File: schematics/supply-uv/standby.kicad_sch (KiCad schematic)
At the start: 106 parts, among them J5 CW2B-10A-T, K1 SRD-12VDC-SL-C, Q1 5N65F, Q2 IRLML5203, Q3 IRLML5203, Q4 IRLML5203, U10 TL331, U2 R7731, U3 EL817, U4 EL817, U5 L7805ABV, U6 L7805ABV, U7 TL431DBZ, U8 EL817, U9 TL432DBZ, Y1 B32022A3223M000

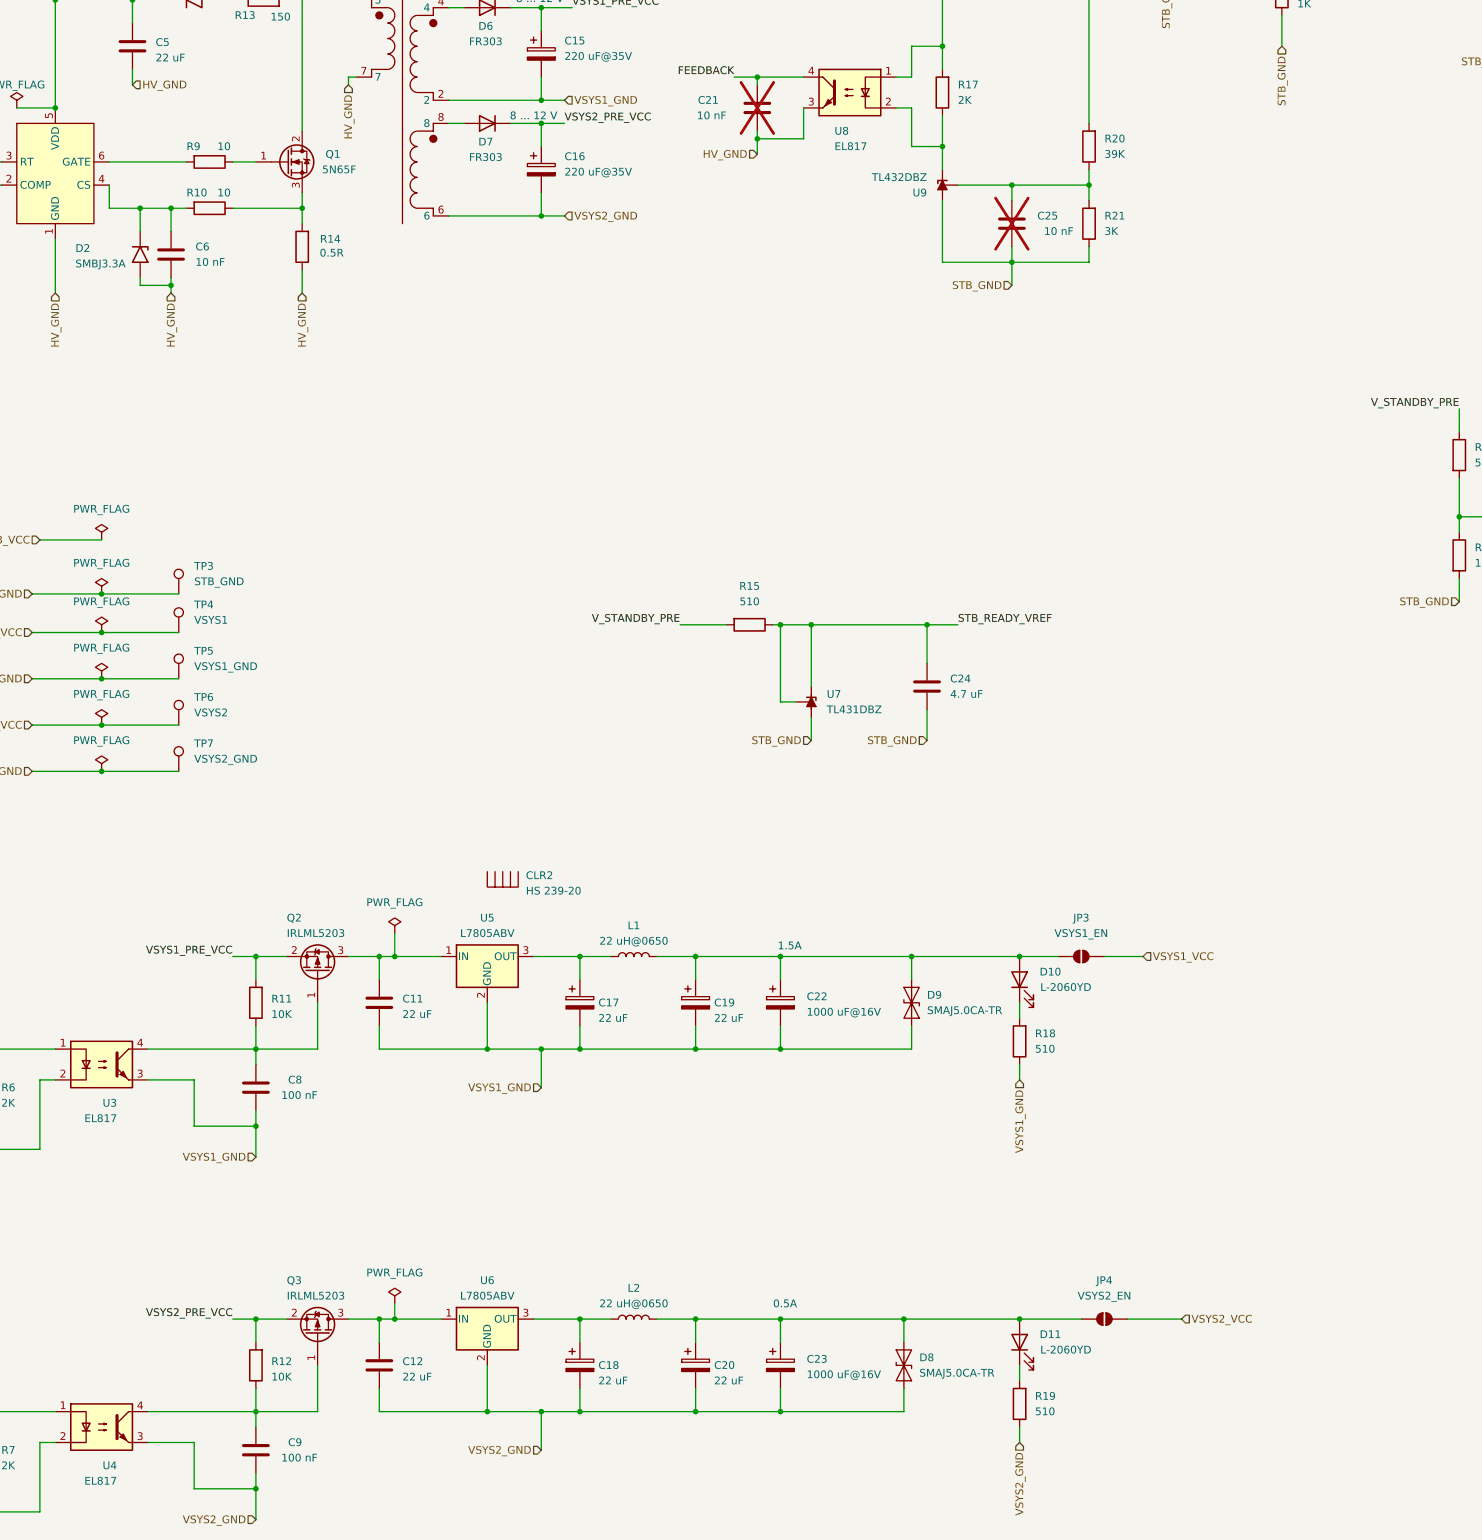
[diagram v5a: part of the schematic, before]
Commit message: some changes in board routing
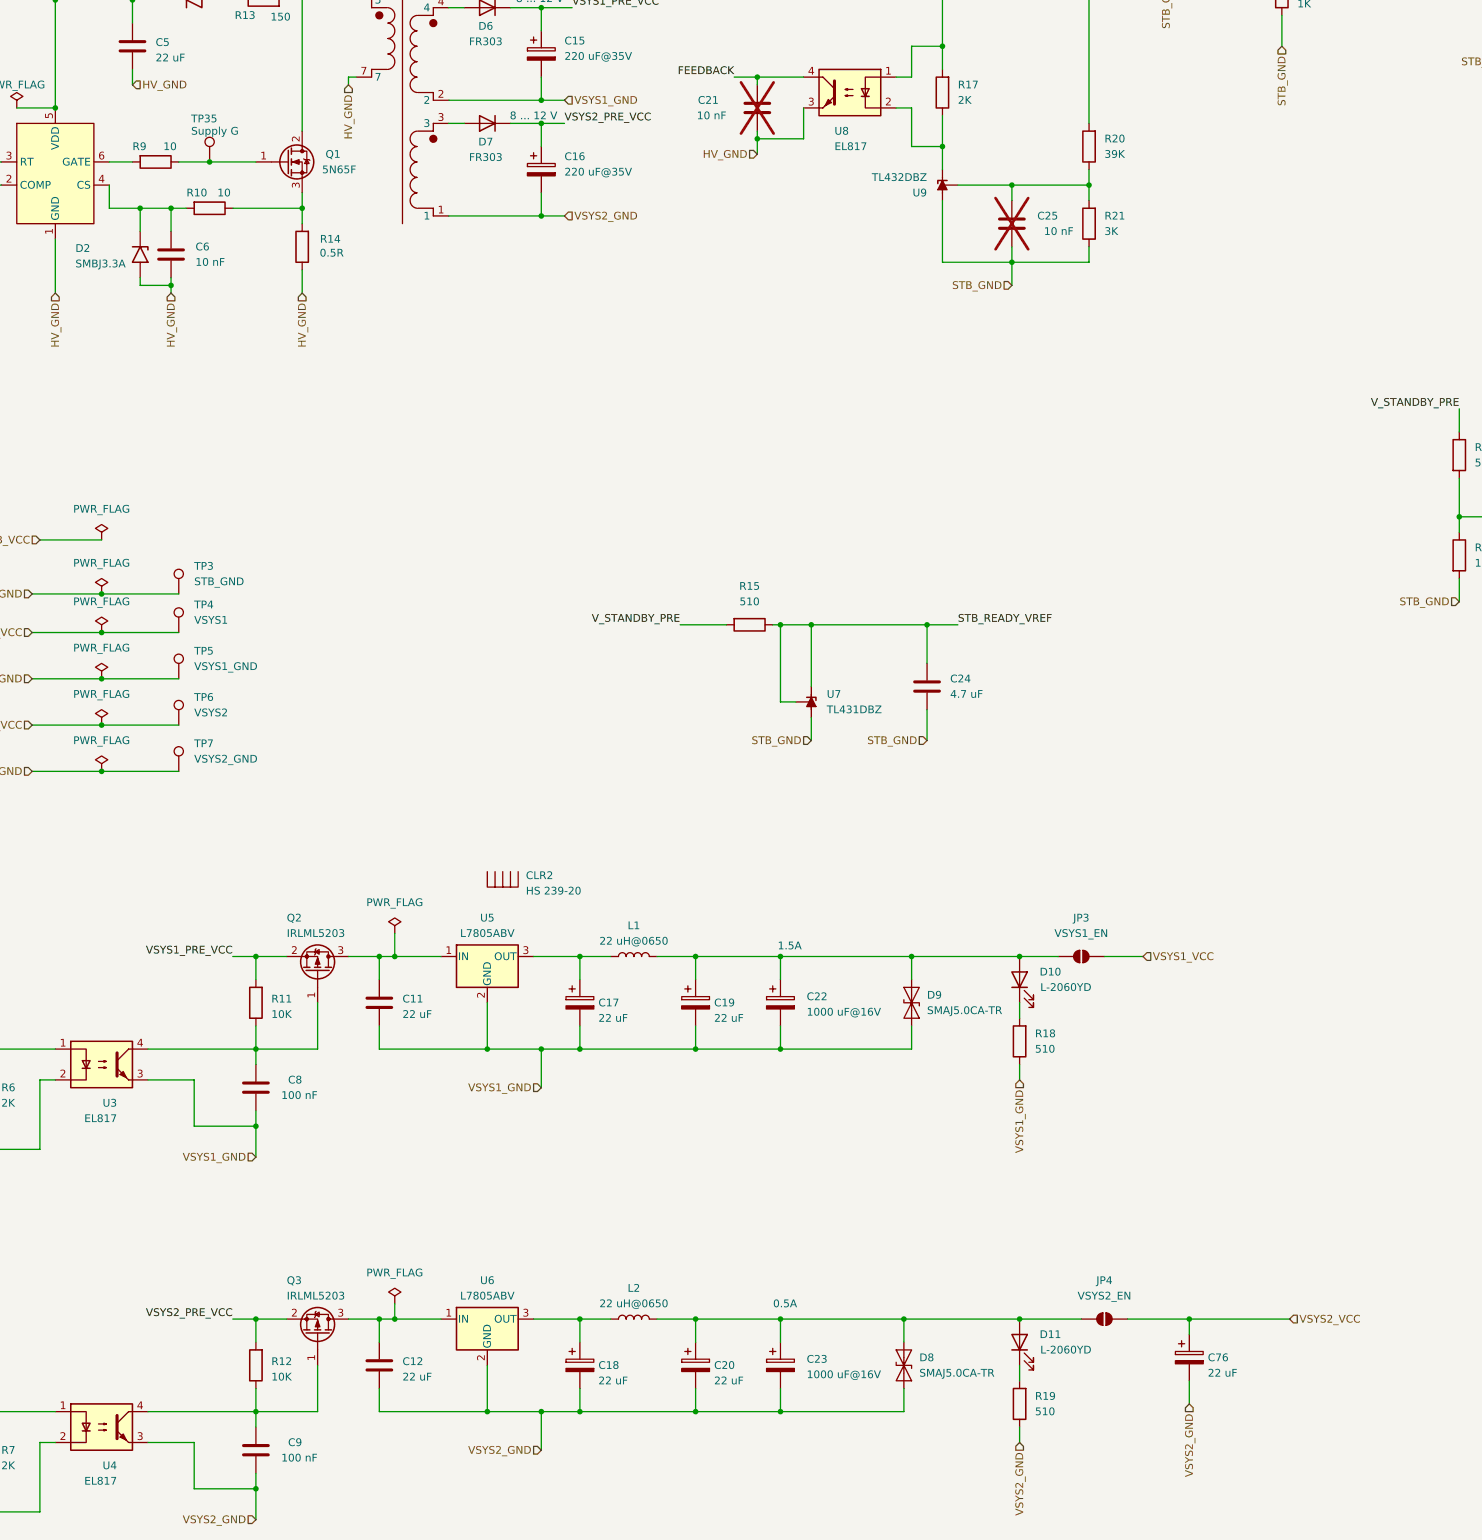
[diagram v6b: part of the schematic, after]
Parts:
- added C76: 22 uF, Capacitor_Tantalum_SMD:CP_EIA-3216-10_Kemet-I_Pad1.58x1.35mm_HandSolder, symbol Device:C_Polarized
- added TP35: Supply G, TestPoint:TestPoint_Pad_1.0x1.0mm, symbol Connector:TestPoint
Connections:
- net VSYS2_GND: now also TR1.1, C76.2; no longer TR1.6
- net VSYS2_VCC: now also C76.1
- net at D7.2 (A): now also TR1.3; no longer TR1.8
- net at Q1.1 (G), R9.1: now also TP35.1
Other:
- moved on the sheet: R9
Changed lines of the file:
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@@
 	)
 	(junction
+		(at 116.84 172.72)
+		(diameter 0)
+		(color 0 0 0 0)
+	)
+	(junction
 		(at 91.44 163.83)
 		(diameter 0)
@@
 	)
 	(junction
+		(at 278.13 363.22)
+		(diameter 0)
+		(color 0 0 0 0)
+	)
+	(junction
 		(at 124.46 331.47)
 		(diameter 0)
@@
 	(wire
 		(pts
+			(xy 116.84 172.72) (xy 124.46 172.72)
+		)
+		(stroke
+			(width 0)
+			(type default)
+		)
+	)
+	(wire
+		(pts
 			(xy 31.75 53.34) (xy 35.56 53.34)
 		)
@@
 	(wire
 		(pts
-			(xy 100.33 172.72) (xy 113.03 172.72)
+			(xy 100.33 172.72) (xy 104.14 172.72)
 		)
 		(stroke
@@
 	(wire
 		(pts
-			(xy 267.97 363.22) (xy 276.86 363.22)
+			(xy 267.97 363.22) (xy 278.13 363.22)
 		)
 		(stroke
@@
 	(wire
 		(pts
+			(xy 278.13 363.22) (xy 294.64 363.22)
+		)
+		(stroke
+			(width 0)
+			(type default)
+		)
+	)
+	(wire
+		(pts
 			(xy 332.74 128.27) (xy 332.74 132.08)
 		)
@@
 	(wire
 		(pts
+			(xy 278.13 363.22) (xy 278.13 365.76)
+		)
+		(stroke
+			(width 0)
+			(type default)
+		)
+	)
+	(wire
+		(pts
 			(xy 124.46 391.16) (xy 124.46 388.62)
 		)
@@
 	(wire
 		(pts
+			(xy 278.13 373.38) (xy 278.13 377.19)
+		)
+		(stroke
+			(width 0)
+			(type default)
+		)
+	)
+	(wire
+		(pts
 			(xy 104.14 41.91) (xy 104.14 43.18)
 		)
@@
 	(wire
 		(pts
-			(xy 120.65 172.72) (xy 124.46 172.72)
+			(xy 111.76 172.72) (xy 116.84 172.72)
 		)
 		(stroke
@@
 		)
 	)
+	(hierarchical_label "VSYS2_GND"
+		(shape input)
+		(at 278.13 377.19 270)
+		(fields_autoplaced yes)
+		(effects
+			(font
+				(size 1.27 1.27)
+			)
+			(justify right)
+		)
+	)
 	(hierarchical_label "VSYS1_GND"
 		(shape input)
@@
 	(hierarchical_label "VSYS2_VCC"
 		(shape input)
-		(at 276.86 363.22 0)
+		(at 294.64 363.22 0)
 		(fields_autoplaced yes)
 		(effects
@@
 		(pin "13"
 		)
-		(pin "6"
+		(pin "1"
 		)
 		(pin "5"
@@
 		(pin "4"
 		)
-		(pin "8"
+		(pin "3"
 		)
 		(pin "2"
@@
 	(symbol
 		(lib_id "Device:R")
-		(at 116.84 172.72 270)
+		(at 107.95 172.72 270)
 		(unit 1)
 		(exclude_from_sim no)
@@
 		(dnp no)
 		(property "Reference" "R9"
-			(at 113.03 170.18 90)
+			(at 104.14 170.18 90)
 			(effects
 				(font
@@
 		)
 		(property "Value" "10"
-			(at 118.11 170.18 90)
+			(at 109.22 170.18 90)
 			(effects
 				(font
@@
 		)
 		(property "Footprint" "Resistor_SMD:R_0805_2012Metric"
-			(at 116.84 170.942 90)
+			(at 107.95 170.942 90)
 			(effects
 				(font
@@
 		)
 		(property "Datasheet" "~"
-			(at 116.84 172.72 0)
+			(at 107.95 172.72 0)
 			(effects
 				(font
@@
 		)
 		(property "Description" "Resistor"
-			(at 116.84 172.72 0)
+			(at 107.95 172.72 0)
 			(effects
 				(font
@@
 	)
 	(symbol
+		(lib_id "Device:C_Polarized")
+		(at 278.13 369.57 0)
+		(unit 1)
+		(exclude_from_sim no)
+		(in_bom yes)
+		(on_board yes)
+		(dnp no)
+		(property "Reference" "C76"
+			(at 281.178 369.57 0)
+			(effects
+				(font
+					(size 1.27 1.27)
+				)
+				(justify left)
+			)
+		)
+		(property "Value" "22 uF"
+			(at 281.178 372.11 0)
+			(effects
+				(font
+					(size 1.27 1.27)
+				)
+				(justify left)
+			)
+		)
+		(property "Footprint" "Capacitor_Tantalum_SMD:CP_EIA-3216-10_Kemet-I_Pad1.58x1.35mm_HandSolder"
+			(at 279.0952 373.38 0)
+			(effects
+				(font
+					(size 1.27 1.27)
+				)
+				(hide yes)
+			)
+		)
+		(property "Datasheet" "~"
+			(at 278.13 369.57 0)
+			(effects
+				(font
+					(size 1.27 1.27)
+				)
+				(hide yes)
+			)
+		)
+		(property "Description" "Polarized capacitor"
+			(at 278.13 369.57 0)
+			(effects
+				(font
+					(size 1.27 1.27)
+				)
+				(hide yes)
+			)
+		)
+		(pin "2"
+		)
+		(pin "1"
+		)
+		(instances
+			(project "supply-uv"
+				(path "/ef40850c-d0bf-4cba-961b-9aba418f8e73/14317b0a-1f8a-4d8b-b159-cbc20c410ffd"
+					(reference "C76")
+					(unit 1)
+				)
+			)
+		)
+	)
+	(symbol
 		(lib_id "Device:R")
 		(at 59.69 182.88 180)
@@
 					(unit 1)
 				)
+			)
+		)
+	)
+	(symbol
+		(lib_id "Connector:TestPoint")
+		(at 116.84 172.72 0)
+		(unit 1)
+		(exclude_from_sim no)
+		(in_bom yes)
+		(on_board yes)
+		(dnp no)
+		(property "Reference" "TP35"
+			(at 113.792 165.608 0)
+			(effects
+				(font
+					(size 1.27 1.27)
+				)
+				(justify left)
+			)
+		)
+		(property "Value" "Supply G"
+			(at 113.792 167.64 0)
+			(effects
+				(font
+					(size 1.27 1.27)
+				)
+				(justify left)
+			)
+		)
+		(property "Footprint" "TestPoint:TestPoint_Pad_1.0x1.0mm"
+			(at 121.92 172.72 0)
+			(effects
+				(font
+					(size 1.27 1.27)
+				)
+				(hide yes)
+			)
+		)
+		(property "Datasheet" "~"
+			(at 121.92 172.72 0)
+			(effects
+				(font
+					(size 1.27 1.27)
+				)
+				(hide yes)
+			)
+		)
+		(property "Description" "test point"
+			(at 116.84 172.72 0)
+			(effects
+				(font
+					(size 1.27 1.27)
+				)
+				(hide yes)
+			)
+		)
+		(pin "1"
+		)
+		(instances
+			(project "supply-uv"
+				(path "/ef40850c-d0bf-4cba-961b-9aba418f8e73/14317b0a-1f8a-4d8b-b159-cbc20c410ffd"
+					(reference "TP35")
+					(unit 1)
+				)
